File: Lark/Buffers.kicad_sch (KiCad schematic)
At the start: 5 parts, among them U10 SN74LVC541ARGYR, U9 SN74LVC2G34DBVR

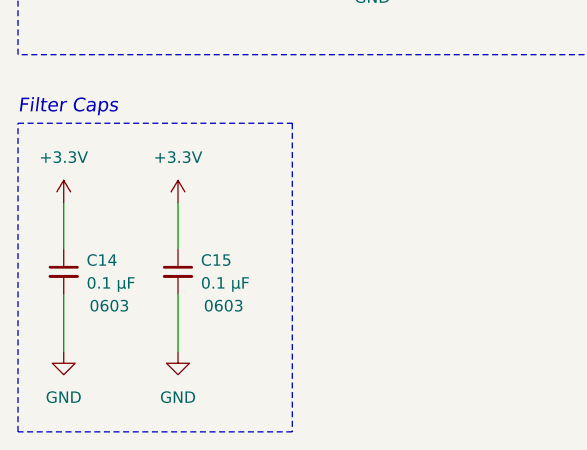
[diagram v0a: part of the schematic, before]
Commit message: added power section to schematic
It needs revised, due to thermal issue. Specifically in regards to my soft start circuit, the mosfet wont be able to handle the power dissipated during a slow turn on.
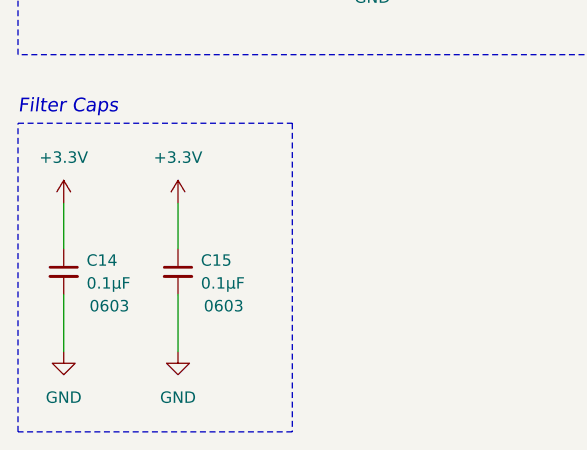
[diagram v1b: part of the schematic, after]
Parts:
- C14, C15: value 0.1 µF -> 0.1µF
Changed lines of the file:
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@@
 			)
 		)
-		(property "Value" "0.1 µF"
+		(property "Value" "0.1µF"
 			(at 25.4 176.5362 0)
 			(effects
@@
 			)
 		)
-		(property "Datasheet" "https://search.murata.co.jp/Ceramy/image/img/A01X/G101/ENG/GRM188R72A104MA35-01A.pdf"
+		(property "Datasheet" "~"
 			(at 22.86 175.26 0)
 			(effects
@@
 			)
 		)
-		(property "Value" "0.1 µF"
+		(property "Value" "0.1µF"
 			(at 38.1 176.5362 0)
 			(effects
@@
 			)
 		)
-		(property "Datasheet" "https://search.murata.co.jp/Ceramy/image/img/A01X/G101/ENG/GRM188R72A104MA35-01A.pdf"
+		(property "Datasheet" "~"
 			(at 35.56 175.26 0)
 			(effects
@@
 			)
 		)
-		(property "Datasheet" "https://www.seielect.com/catalog/SEI-RMCF_RMCP.pdf"
+		(property "Datasheet" "~"
 			(at 52.07 40.64 0)
 			(effects

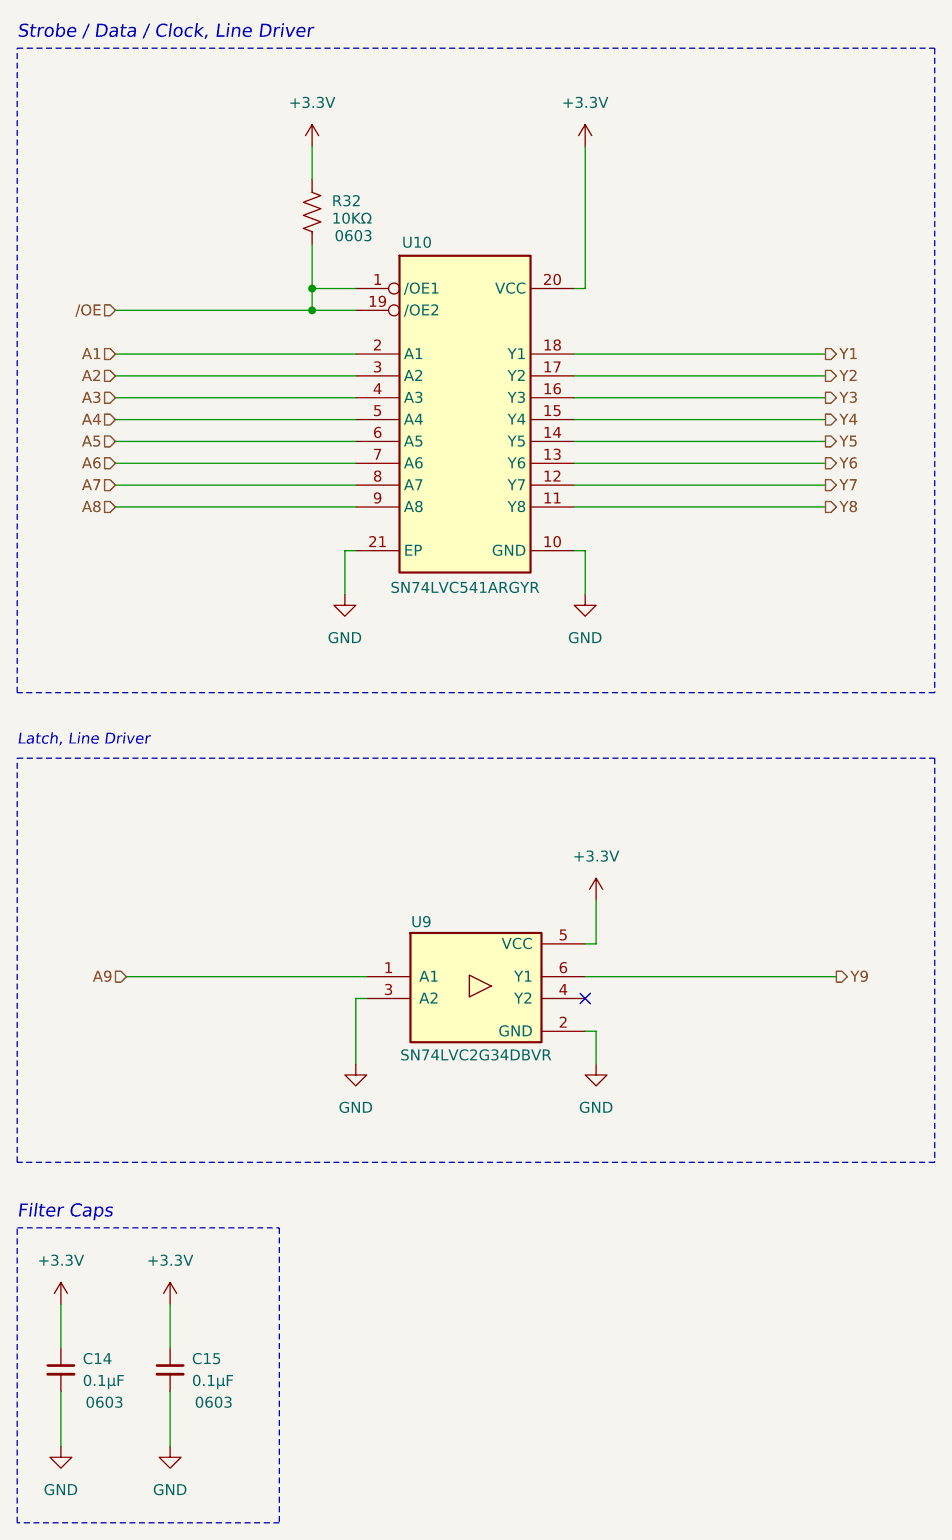
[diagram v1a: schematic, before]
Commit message: update, WIP
- Reannotated schematic.
- Added STM32 device.
- Fixed High-side switch (removed soft-start cap for device safety).
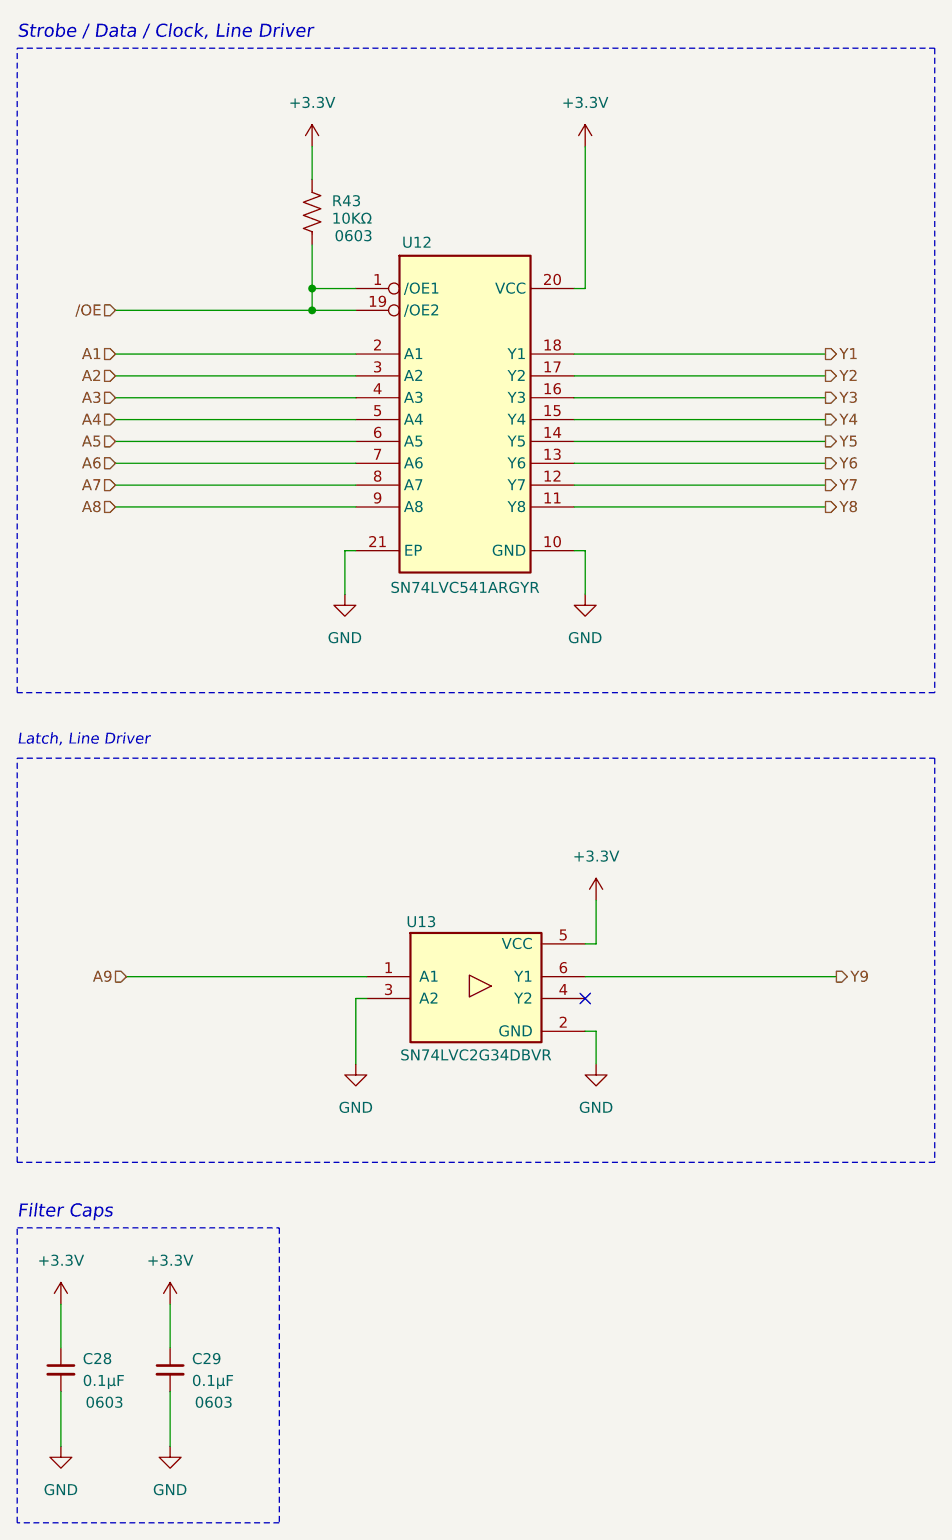
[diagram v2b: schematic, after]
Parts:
- renumbered C14 to C28, C15 to C29, R32 to R43, U10 to U12, U9 to U13
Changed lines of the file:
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@@
 		(on_board yes)
 		(dnp no)
-		(property "Reference" "U9"
+		(property "Reference" "U13"
 			(at 64.77 123.19 0)
 			(effects
@@
 			(project ""
 				(path "/a351af57-4353-47da-9f45-7393de572768/6e291d34-e508-4d3b-a2e9-20acfef2b928/cf6d8bd3-7897-4dde-81d8-03d5b6d87e30"
-					(reference "U9")
+					(reference "U13")
 					(unit 1)
 				)
@@
 		(dnp no)
 		(fields_autoplaced yes)
-		(property "Reference" "#PWR076"
+		(property "Reference" "#PWR0124"
 			(at 85.09 124.46 0)
 			(effects
@@
 			(project "Lark"
 				(path "/a351af57-4353-47da-9f45-7393de572768/6e291d34-e508-4d3b-a2e9-20acfef2b928/cf6d8bd3-7897-4dde-81d8-03d5b6d87e30"
-					(reference "#PWR076")
+					(reference "#PWR0124")
 					(unit 1)
 				)
@@
 		(dnp no)
 		(fields_autoplaced yes)
-		(property "Reference" "#PWR082"
+		(property "Reference" "#PWR0130"
 			(at 35.56 190.5 0)
 			(effects
@@
 			(project "Lark"
 				(path "/a351af57-4353-47da-9f45-7393de572768/6e291d34-e508-4d3b-a2e9-20acfef2b928/cf6d8bd3-7897-4dde-81d8-03d5b6d87e30"
-					(reference "#PWR082")
+					(reference "#PWR0130")
 					(unit 1)
 				)
@@
 		(dnp no)
 		(fields_autoplaced yes)
-		(property "Reference" "#PWR077"
+		(property "Reference" "#PWR0126"
 			(at 85.09 146.05 0)
 			(effects
@@
 			(project "Lark"
 				(path "/a351af57-4353-47da-9f45-7393de572768/6e291d34-e508-4d3b-a2e9-20acfef2b928/cf6d8bd3-7897-4dde-81d8-03d5b6d87e30"
-					(reference "#PWR077")
+					(reference "#PWR0126")
 					(unit 1)
 				)
@@
 		(dnp no)
 		(fields_autoplaced yes)
-		(property "Reference" "#PWR078"
+		(property "Reference" "#PWR0125"
 			(at 57.15 146.05 0)
 			(effects
@@
 			(project "Lark"
 				(path "/a351af57-4353-47da-9f45-7393de572768/6e291d34-e508-4d3b-a2e9-20acfef2b928/cf6d8bd3-7897-4dde-81d8-03d5b6d87e30"
-					(reference "#PWR078")
+					(reference "#PWR0125")
 					(unit 1)
 				)
@@
 		(dnp no)
 		(fields_autoplaced yes)
-		(property "Reference" "#PWR080"
+		(property "Reference" "#PWR0129"
 			(at 22.86 190.5 0)
 			(effects
@@
 			(project "Lark"
 				(path "/a351af57-4353-47da-9f45-7393de572768/6e291d34-e508-4d3b-a2e9-20acfef2b928/cf6d8bd3-7897-4dde-81d8-03d5b6d87e30"
-					(reference "#PWR080")
+					(reference "#PWR0129")
 					(unit 1)
 				)
@@
 		(on_board yes)
 		(dnp no)
-		(property "Reference" "C14"
+		(property "Reference" "C28"
 			(at 25.4 173.9962 0)
 			(effects
@@
 			(project "Lark"
 				(path "/a351af57-4353-47da-9f45-7393de572768/6e291d34-e508-4d3b-a2e9-20acfef2b928/cf6d8bd3-7897-4dde-81d8-03d5b6d87e30"
-					(reference "C14")
+					(reference "C28")
 					(unit 1)
 				)
@@
 		(dnp no)
 		(fields_autoplaced yes)
-		(property "Reference" "#PWR079"
+		(property "Reference" "#PWR0127"
 			(at 22.86 171.45 0)
 			(effects
@@
 			(project "Lark"
 				(path "/a351af57-4353-47da-9f45-7393de572768/6e291d34-e508-4d3b-a2e9-20acfef2b928/cf6d8bd3-7897-4dde-81d8-03d5b6d87e30"
-					(reference "#PWR079")
+					(reference "#PWR0127")
 					(unit 1)
 				)
@@
 		(on_board yes)
 		(dnp no)
-		(property "Reference" "C15"
+		(property "Reference" "C29"
 			(at 38.1 173.9962 0)
 			(effects
@@
 			(project "Lark"
 				(path "/a351af57-4353-47da-9f45-7393de572768/6e291d34-e508-4d3b-a2e9-20acfef2b928/cf6d8bd3-7897-4dde-81d8-03d5b6d87e30"
-					(reference "C15")
+					(reference "C29")
 					(unit 1)
 				)
@@
 		(dnp no)
 		(fields_autoplaced yes)
-		(property "Reference" "#PWR072"
+		(property "Reference" "#PWR0121"
 			(at 83.82 36.83 0)
 			(effects
@@
 			(project "Lark"
 				(path "/a351af57-4353-47da-9f45-7393de572768/6e291d34-e508-4d3b-a2e9-20acfef2b928/cf6d8bd3-7897-4dde-81d8-03d5b6d87e30"
-					(reference "#PWR072")
+					(reference "#PWR0121")
 					(unit 1)
 				)
@@
 		(dnp no)
 		(fields_autoplaced yes)
-		(property "Reference" "#PWR075"
+		(property "Reference" "#PWR0120"
 			(at 52.07 36.83 0)
 			(effects
@@
 			(project "Lark"
 				(path "/a351af57-4353-47da-9f45-7393de572768/6e291d34-e508-4d3b-a2e9-20acfef2b928/cf6d8bd3-7897-4dde-81d8-03d5b6d87e30"
-					(reference "#PWR075")
+					(reference "#PWR0120")
 					(unit 1)
 				)
@@
 		(dnp no)
 		(fields_autoplaced yes)
-		(property "Reference" "#PWR081"
+		(property "Reference" "#PWR0128"
 			(at 35.56 171.45 0)
 			(effects
@@
 			(project "Lark"
 				(path "/a351af57-4353-47da-9f45-7393de572768/6e291d34-e508-4d3b-a2e9-20acfef2b928/cf6d8bd3-7897-4dde-81d8-03d5b6d87e30"
-					(reference "#PWR081")
+					(reference "#PWR0128")
 					(unit 1)
 				)
@@
 		(on_board yes)
 		(dnp no)
-		(property "Reference" "R32"
+		(property "Reference" "R43"
 			(at 54.356 39.37 0)
 			(effects
@@
 			(project "Lark"
 				(path "/a351af57-4353-47da-9f45-7393de572768/6e291d34-e508-4d3b-a2e9-20acfef2b928/cf6d8bd3-7897-4dde-81d8-03d5b6d87e30"
-					(reference "R32")
+					(reference "R43")
 					(unit 1)
 				)
@@
 		(on_board yes)
 		(dnp no)
-		(property "Reference" "U10"
+		(property "Reference" "U12"
 			(at 64.262 44.196 0)
 			(effects
@@
 			(project ""
 				(path "/a351af57-4353-47da-9f45-7393de572768/6e291d34-e508-4d3b-a2e9-20acfef2b928/cf6d8bd3-7897-4dde-81d8-03d5b6d87e30"
-					(reference "U10")
+					(reference "U12")
 					(unit 1)
 				)
@@
 		(dnp no)
 		(fields_autoplaced yes)
-		(property "Reference" "#PWR073"
+		(property "Reference" "#PWR0123"
 			(at 83.82 91.44 0)
 			(effects
@@
 			(project "Lark"
 				(path "/a351af57-4353-47da-9f45-7393de572768/6e291d34-e508-4d3b-a2e9-20acfef2b928/cf6d8bd3-7897-4dde-81d8-03d5b6d87e30"
-					(reference "#PWR073")
+					(reference "#PWR0123")
 					(unit 1)
 				)
@@
 		(dnp no)
 		(fields_autoplaced yes)
-		(property "Reference" "#PWR074"
+		(property "Reference" "#PWR0122"
 			(at 55.88 91.44 0)
 			(effects
@@
 			(project "Lark"
 				(path "/a351af57-4353-47da-9f45-7393de572768/6e291d34-e508-4d3b-a2e9-20acfef2b928/cf6d8bd3-7897-4dde-81d8-03d5b6d87e30"
-					(reference "#PWR074")
-					(unit 1)
-				)
+					(reference "#PWR0122")
+					(unit 1)
+				)

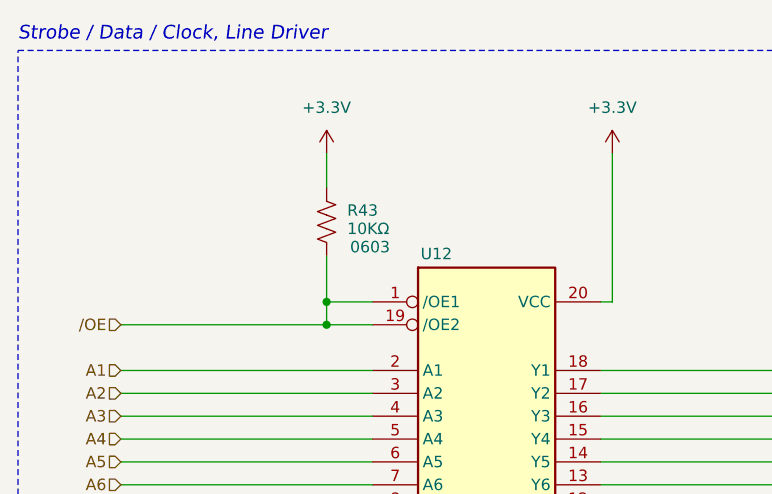
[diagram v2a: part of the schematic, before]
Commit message: Updated schematic, WIP
- Added NOR flash part.
- Added new CubeMX config file.
- Reannotated the schematic.
- Made some more connections to the MCU.
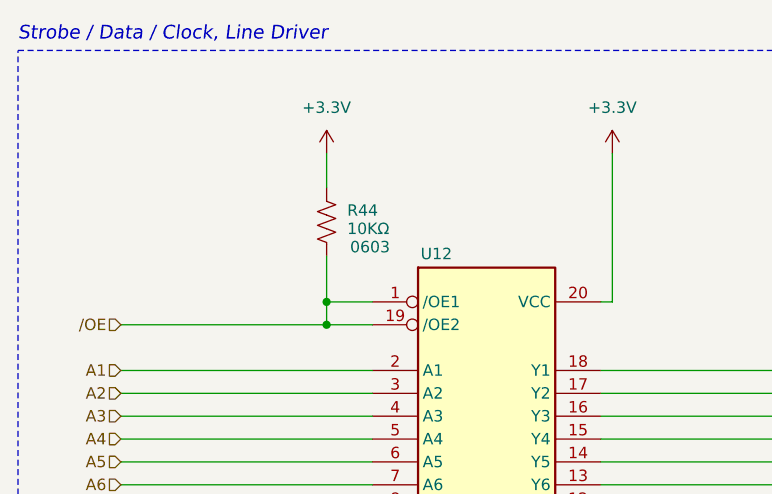
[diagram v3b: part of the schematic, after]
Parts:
- renumbered R43 to R44
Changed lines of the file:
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@@
 		(on_board yes)
 		(dnp no)
-		(property "Reference" "R43"
+		(property "Reference" "R44"
 			(at 54.356 39.37 0)
 			(effects
@@
 			(project "Lark"
 				(path "/a351af57-4353-47da-9f45-7393de572768/6e291d34-e508-4d3b-a2e9-20acfef2b928/cf6d8bd3-7897-4dde-81d8-03d5b6d87e30"
-					(reference "R43")
+					(reference "R44")
 					(unit 1)
 				)

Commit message: Update, WIP
- Added TVS diode to 24v Supply.
- Fixed bleeder circuit at some point (I think it was this commit)
- Added Jumper to connect NTC to ADC. (again I think it was this commit)
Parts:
- renumbered R44 to R47
